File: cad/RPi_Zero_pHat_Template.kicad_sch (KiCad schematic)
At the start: 85 parts, among them J101 Conn_01x03, J102 Conn_01x03, J103 Conn_01x03, J104 Conn_01x03, J105 Conn_01x03, J106 Conn_01x03, J107 Conn_01x03, J108 Conn_02x05_Odd_Even, J109 Conn_01x02, J110 Conn_01x02, J111 Conn_01x04, J112 USB_A, J113 Conn_02x05_Odd_Even, J114 power_input, J115 RPi_GPIO, J116 Conn_02x10_Odd_Even, U1 MCP23017, U101 ASSR-1218, U102 ASSR-1218, U103 ASSR-1218, U104 ASSR-1218, U105 ASSR-1218, U106 ASSR-1218, U107 ASSR-1218, U108 ASSR-1218, U109 ASSR-1218, U110 ASSR-1218, U111 ASSR-1218, U112 ASSR-1218, U113 ASSR-1218, U114 ASSR-1218, U115 ASSR-1218, U116 ASSR-1218

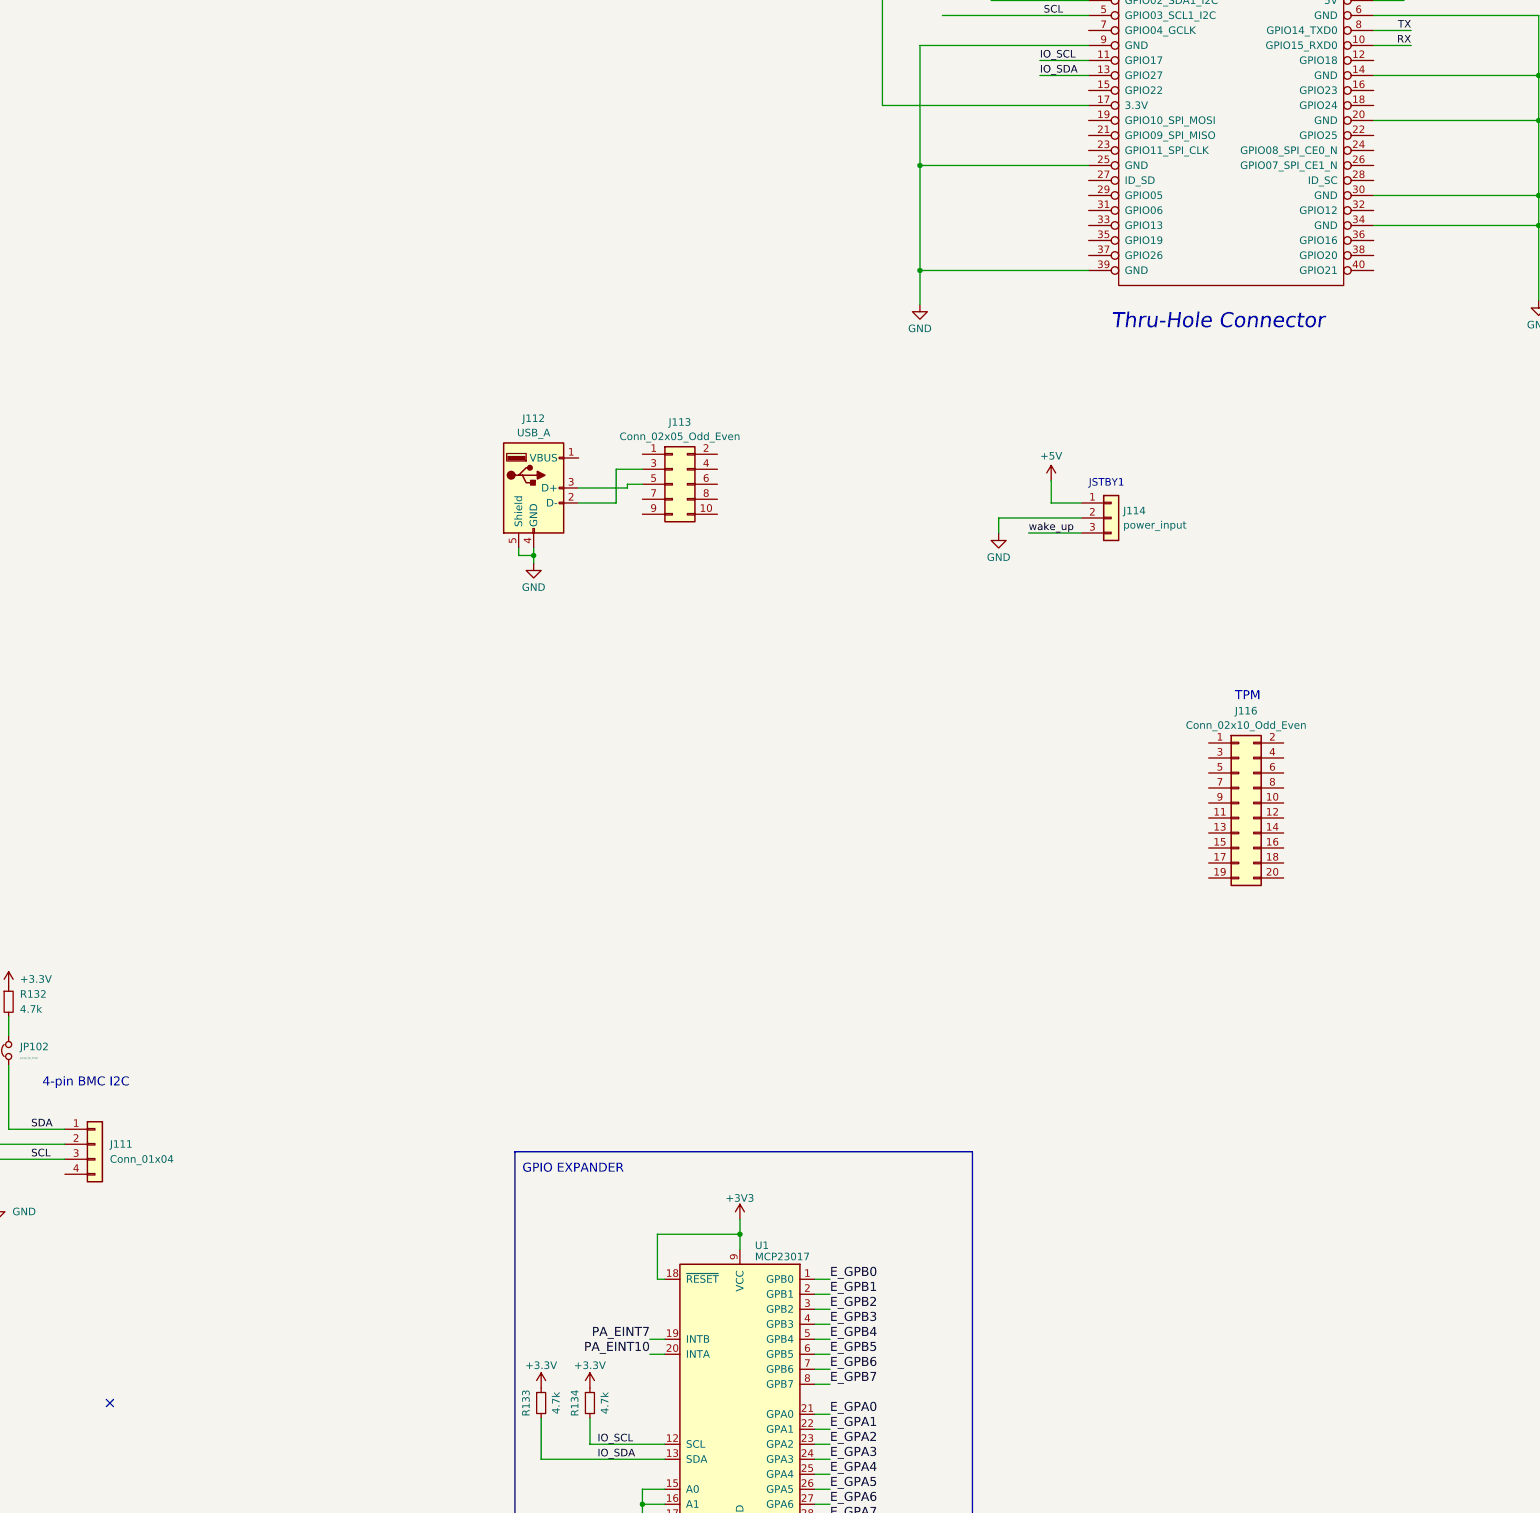
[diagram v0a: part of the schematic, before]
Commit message: move spi pins
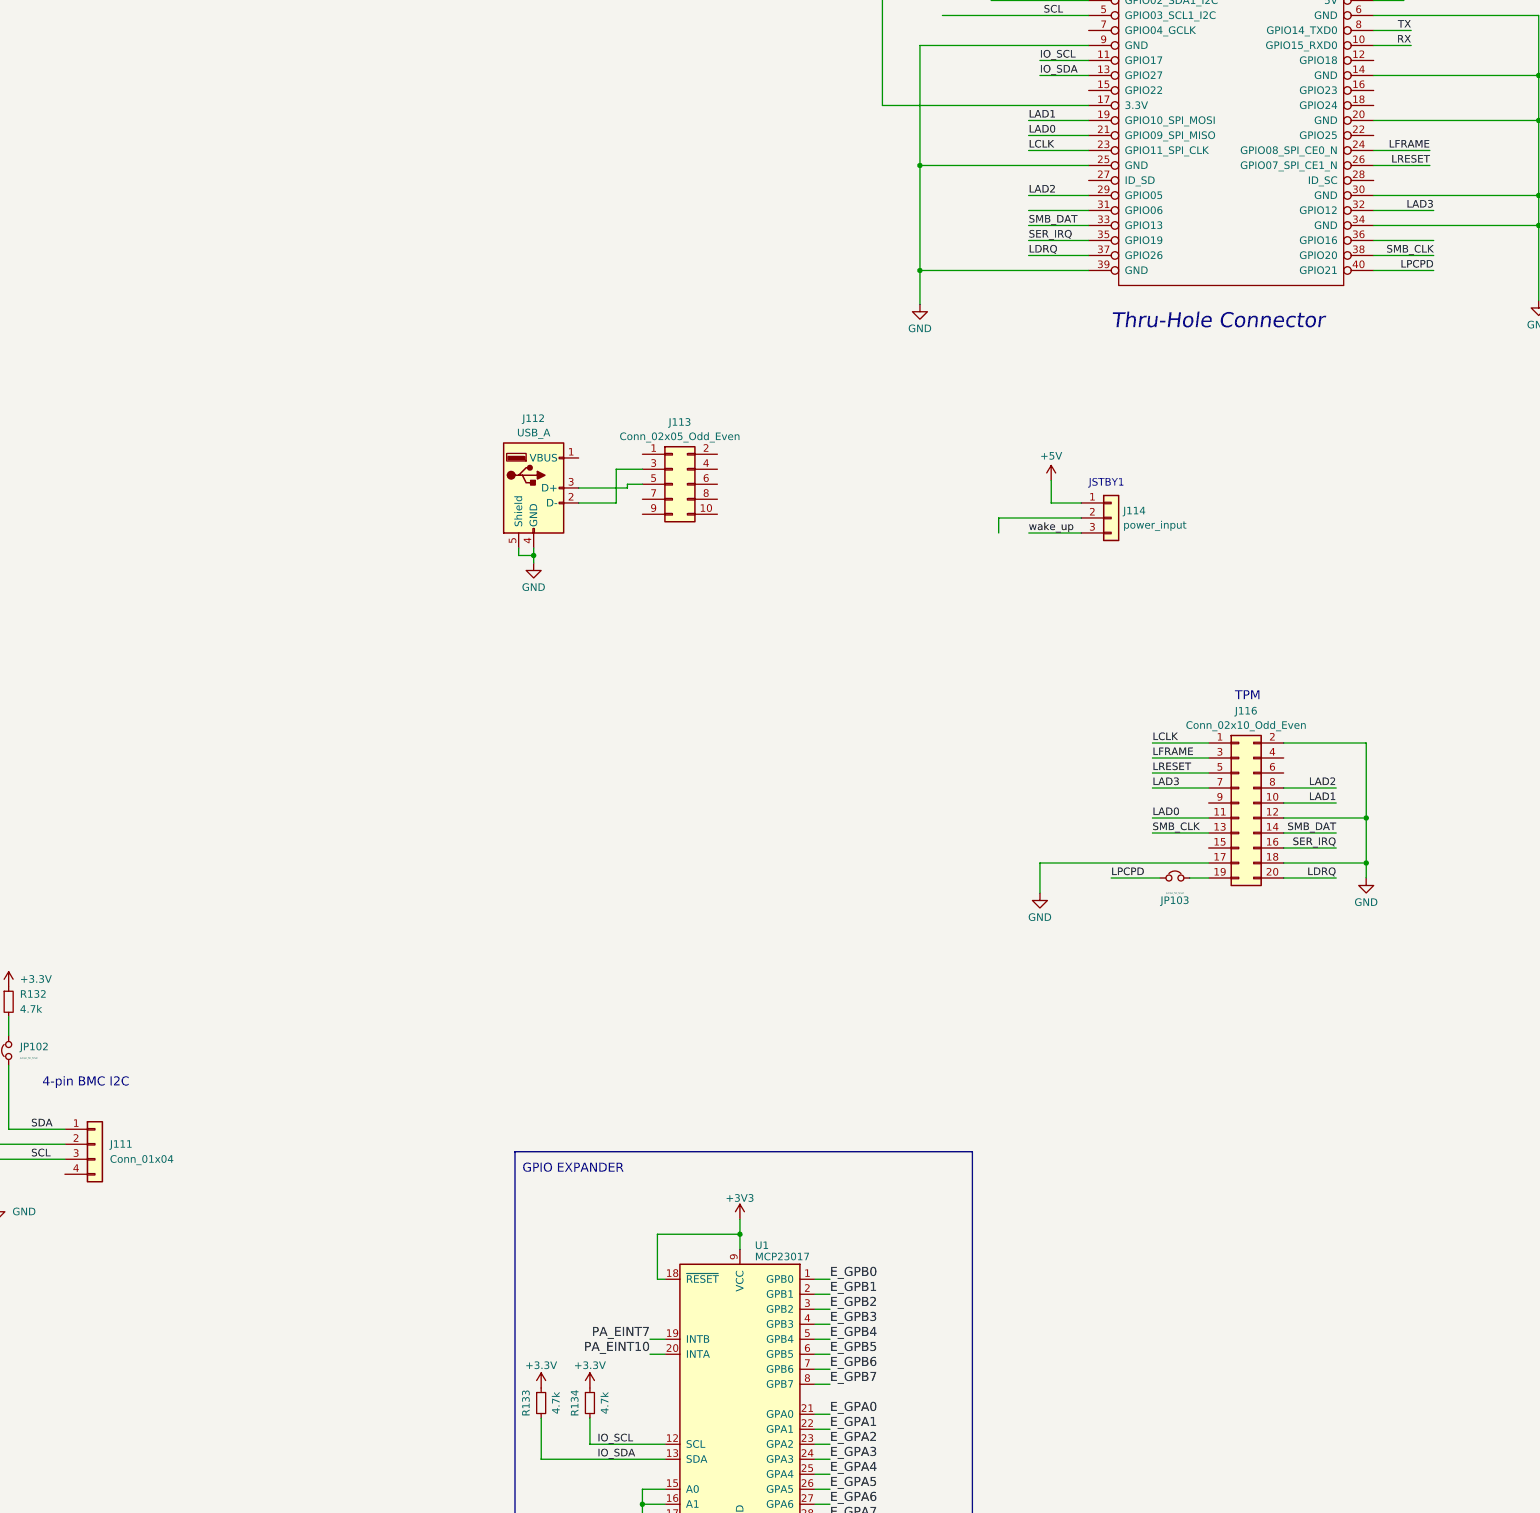
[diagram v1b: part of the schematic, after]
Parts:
- added JP103: Jumper_NC_Small, Jumper:SolderJumper-2_P1.3mm_Bridged_RoundedPad1.0x1.5mm, symbol Device:Jumper_NC_Small
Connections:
- net GND: now also J116.12 (Pin_12), J116.17 (Pin_17), J116.18 (Pin_18), J116.2 (Pin_2); no longer J114.2 (Pin_2)
- net LAD1: now reaches J115.19 (GPIO10_SPI_MOSI)
- net LAD1: now also J116.10 (Pin_10)
- net LAD0: now reaches J115.21 (GPIO09_SPI_MISO)
- net LAD0: now also J116.11 (Pin_11)
- net LCLK: now reaches J115.23 (GPIO11_SPI_CLK)
- net LCLK: now also J116.1 (Pin_1)
- net LFRAME: now reaches J115.24 (GPIO08_SPI_CE0_N)
- net LFRAME: now also J116.3 (Pin_3)
- net LRESET: now reaches J115.26 (GPIO07_SPI_CE1_N)
- net LRESET: now also J116.5 (Pin_5)
- net LAD2: now reaches J115.29 (GPIO05)
- net LAD2: now also J116.8 (Pin_8)
- net LAD3: now reaches J115.32 (GPIO12)
- net LAD3: now also J116.7 (Pin_7)
- net SMB_DAT: now reaches J115.33 (GPIO13)
- net SMB_DAT: now also J116.14 (Pin_14)
- net SER_IRQ: now reaches J115.35 (GPIO19)
- net SER_IRQ: now also J116.16 (Pin_16)
- net LDRQ: now reaches J115.37 (GPIO26)
- net LDRQ: now also J116.20 (Pin_20)
- net SMB_CLK: now reaches J115.38 (GPIO20)
- net SMB_CLK: now also J116.13 (Pin_13)
- net LPCPD: now reaches J115.40 (GPIO21)
- net LPCPD: now also JP103.1
- net at J116.19 (Pin_19): now also JP103.2
- no-connect marks 1 -> 0
